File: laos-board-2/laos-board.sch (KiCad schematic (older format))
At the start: 66 parts, among them IC1 KB847, IC2 KB847, J1 CONN_4, J10 MBED NXP, J11 JP_3, J12 POLOLU1201, J13 CONN_5, J14 CONN_4, J15 JP_3, J16 POLOLU1201, J17 CONN_5, J18 CONN_4, J19 CONN_4, J2 JP, J20 JP, J21 JP, J22 CONN_2, J23 CONN_4, J24 CONN_4, J25 JP, J26 CONN_2, J3 CONN_2, J4 USB-A, J5 MAGJACK, J6 JP_3, J7 POLOLU1201, J8 CONN_5, J9 CONN_4, U1 65HVD251, U2 SDCARD, U3 7805

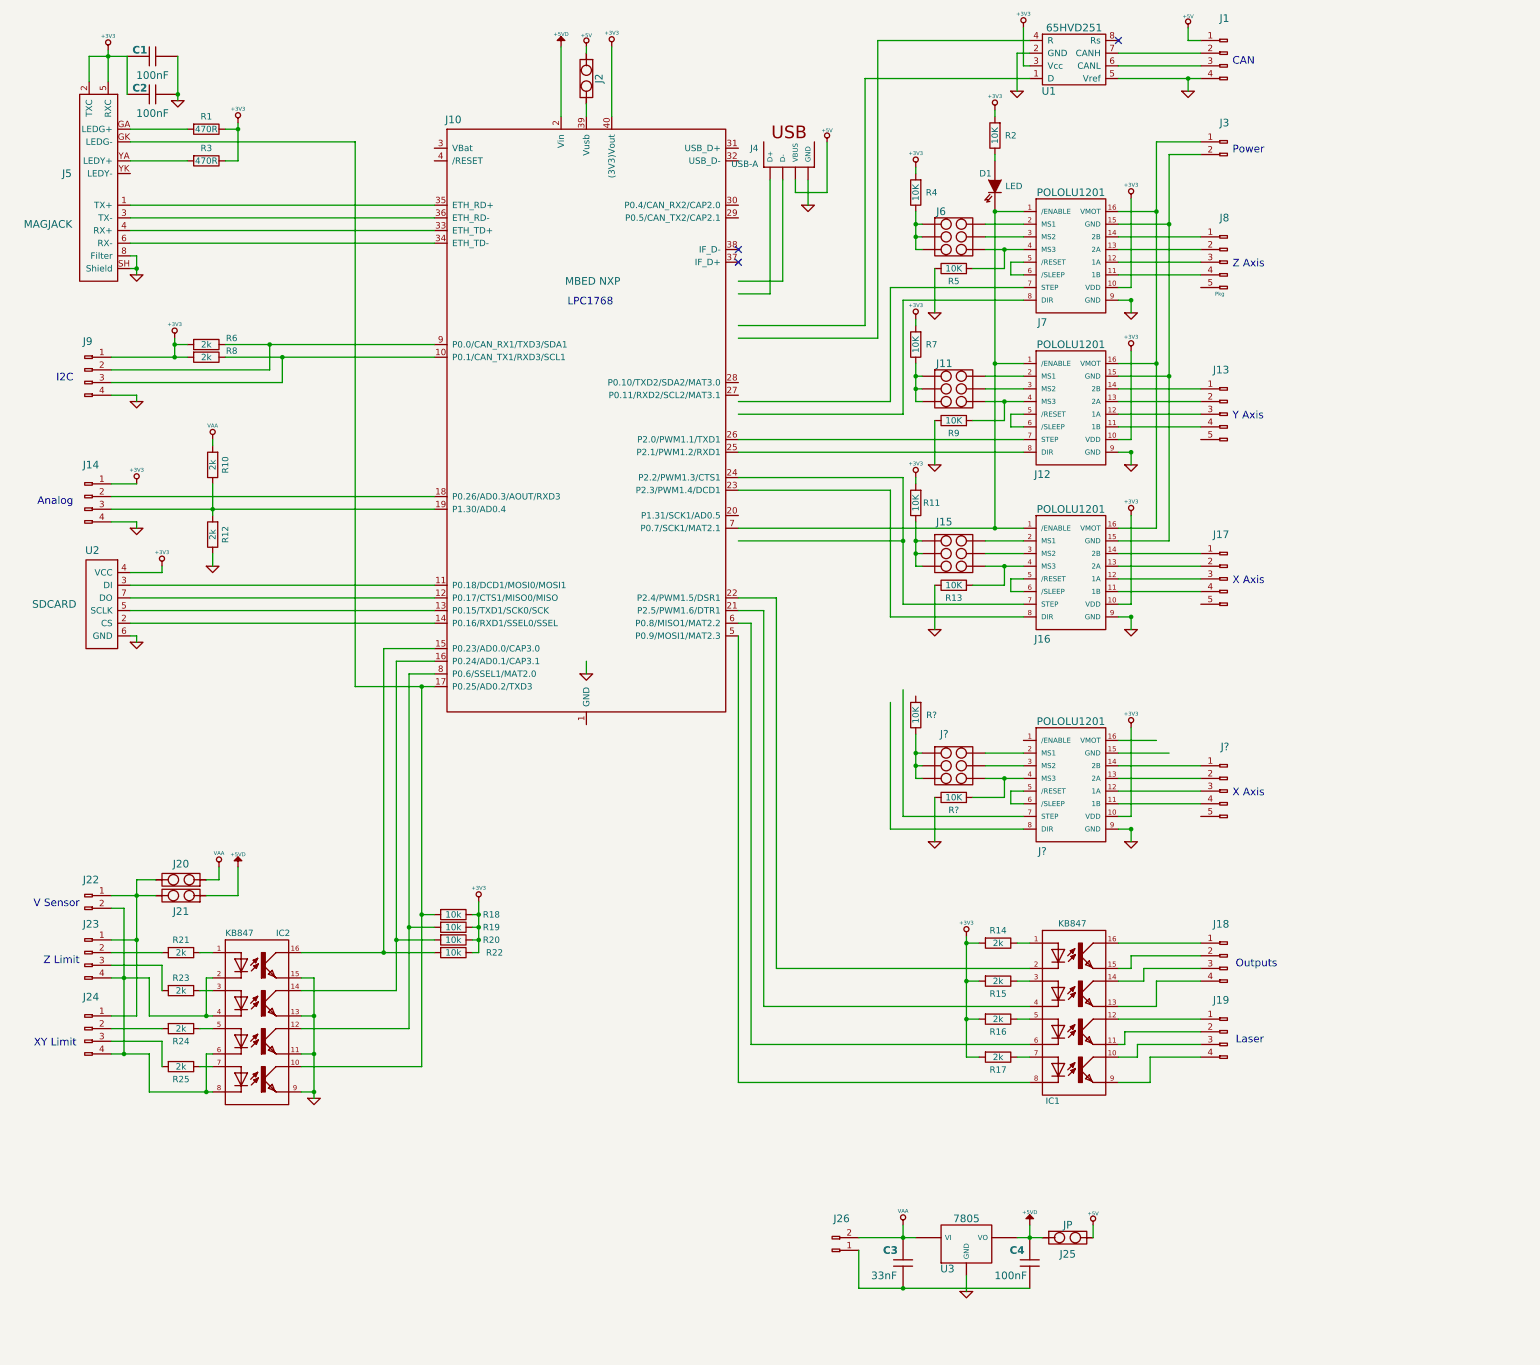
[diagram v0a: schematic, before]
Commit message: Add new polulu and some power nets
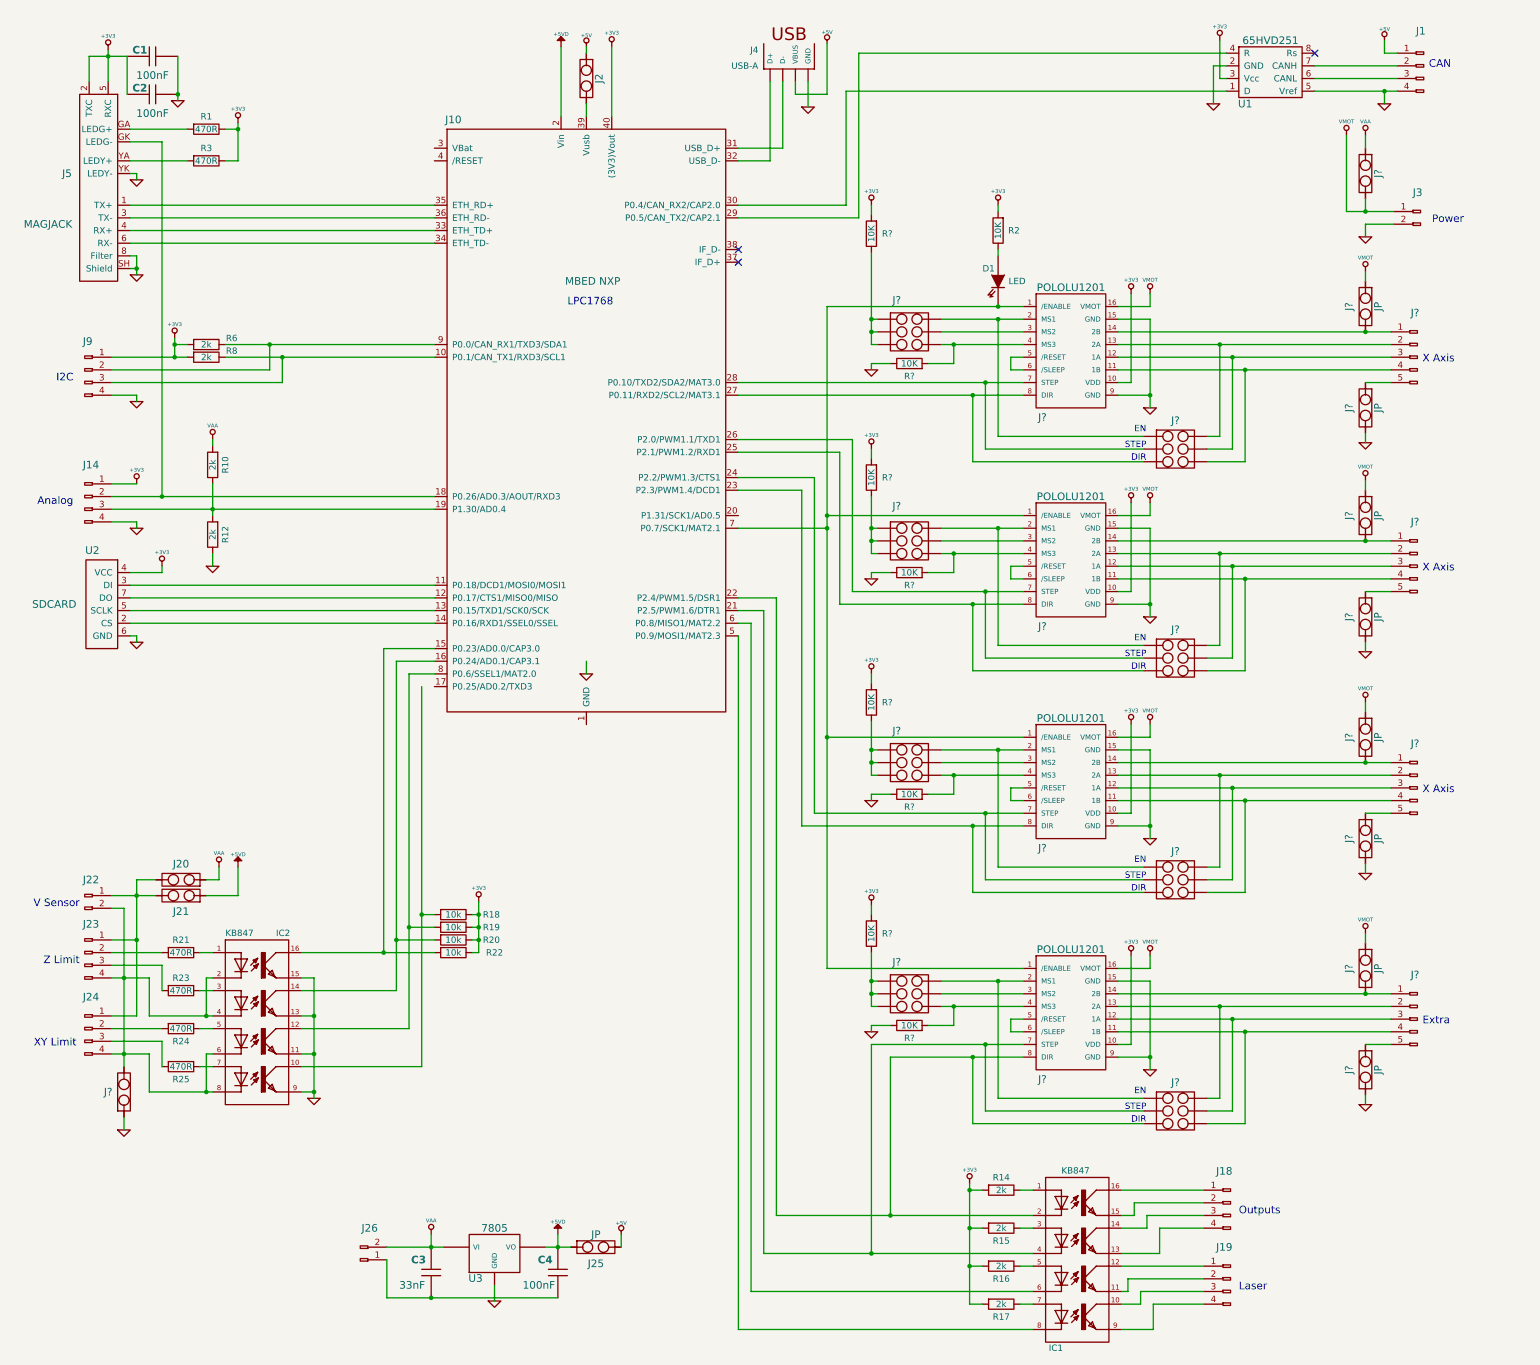
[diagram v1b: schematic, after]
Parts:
- removed J11, J15, J6: JP_3, Pkg, symbol JP_3
- removed J12, J16, J7: POLOLU1201, symbol POLOLU1201
- removed J13, J17, J8: CONN_5, Pkg, symbol CONN_5
- removed R11, R13, R4, R5, R7, R9: 10K, symbol R
- added J? (x10): JP, symbol JP
- added J? (x7): JP_3, Pkg, symbol JP_3
- added J? (x3): POLOLU1201, symbol POLOLU1201
- added J? (x3): CONN_5, Pkg, symbol CONN_5
- added R? (x6): 10K, symbol R
- R21, R23, R24, R25: value 2k -> 470R
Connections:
- net labels added: VMOT
- wire segments 303 -> 377
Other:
- note added: "DIR"
- note added: "EN"
- note added: "Extra"
- note added: "STEP"
- note removed: "Y Axis"
- note removed: "Z Axis"
- moved on the sheet: C3, C4, D1, IC1, J1, J18, J19, J25, J26, J3, J4, J?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

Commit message: Laos board 2 schematic completed before check
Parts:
- added C3: 100nF, Pkg, symbol C
- added C4, C5: 100uF, Pkg, symbol CAP_POL
- gave numbers to parts that had none: 34
- renumbered C3 to C6, C4 to C7, IC2 to IC1, IC1 to IC2, J4 to J1, J9 to J11, J10 to J12, J14 to J15, J1 to J2, J20 to J27, J21 to J29, J2 to J3, J22 to J30, J23 to J31, J24 to J36, J18 to J40, J25 to J41, J26 to J42, J19 to J43, J3 to J6, R12 to R10, R18 to R14, R19 to R15, R20 to R17, R21 to R18, R22 to R19, R3 to R2, R23 to R20, R24 to R22, R25 to R23, R14 to R24, R15 to R25, R16 to R26, R17 to R27, R2 to R3, R6 to R5, R8 to R6, R10 to R8
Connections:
- net GND: now also C3.1, C4.-
- net VMOT: now also C3.2, C4.+
- net at J12.20 (P1.31/SCK1/AD0.5): now also J18.1 (/ENABLE)
- net at D1.2 (K), J12.7 (P0.7/SCK1/MAT2.1), J24.1 (/ENABLE)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: no longer J18.1 (/ENABLE)
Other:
- note added: "Y Axis"
- note added: "Z Axis"
- moved on the sheet: D1, IC2, J10, J13, J14, J16, J17, J18, J19, J2, J20, J21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

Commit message: Updates before pcb design
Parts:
- removed J30: CONN_2, Pkg, symbol CONN_2
- removed J38, J4, J41: JP, symbol JP
- added C?: 100nF, Pkg, symbol C
- added D2: LEDY, symbol LED
- added D3: LEDG, symbol LED
- added J?: CONN_4, Pkg, symbol CONN_4
- added Q? (x2): TIP115, T220-3, symbol TIP115
- added R27, R? (x2): 1k, symbol R
- added R4: 10K, symbol R
- D1: value LED -> LEDR
- R11: renamed from R10; value 2k -> 1k
- R9: renamed from R8; value 2k -> 10k
- renumbered J11 to J10, J12 to J11, J13 to J12, J14 to J13, J15 to J14, J16 to J15, J17 to J16, J18 to J17, J19 to J18, J20 to J19, J21 to J20, J22 to J21, J23 to J22, J24 to J23, J25 to J24, J26 to J25, J27 to J26, J28 to J27, J29 to J28, J31 to J30, J32 to J31, J33 to J32, J34 to J33, J35 to J34, J36 to J35, J37 to J36, J39 to J37, J40 to J38, J42 to J39, J5 to J4, J43 to J40, J6 to J5, J7 to J6, J8 to J7, J9 to J8, J10 to J9, R9 to R10, R11 to R12, R12 to R13, R13 to R14, R14 to R15, R15 to R16, R16 to R17, R17 to R18, R18 to R20, R20 to R21, R21 to R22, R22 to R23, R23 to R24, R24 to R25, R25 to R26, R26 to R28, R27 to R29, R4 to R5, R5 to R6, R6 to R7, R7 to R8
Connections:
- net +5V: now also C7.2, J28.1, U3.3 (VO), R27.1
- net +5VD: no longer C7.2, J28.1, U3.3 (VO)
- net GND: now also J11.1 (GND), J30.4 (P4), J35.4 (P4), C?.1, D2.2 (K), J?.4 (P4), Q?.E, Q?.E
- net VAA: now also C5.+, J39.1 (P1); no longer J39.2 (P2), R9.2
- net VMOT: now also R9.2, R4.2
- net at J11.17 (P0.25/AD0.2/TXD3): now also IC1.10, R15.2
- net at J11.31 (USB_D+): now also J1.D+; no longer J1.D-
- net at J11.32 (USB_D-): now also J1.D-; no longer J1.D+
- net at IC2.8, J11.5 (P0.9/MOSI1/MAT2.3): now also R?.1
- net at IC2.6, J11.6 (P0.8/MISO1/MAT2.2): now also R?.1
- net at C6.1, C7.1: now also C5.-, J39.2 (P2), D3.2 (K); no longer J39.1 (P1)
- net at IC1.1: now also IC1.3 (A), IC1.5, IC1.7, J26.2, J28.2, J30.1 (P1), J35.1 (P1), J?.3 (P3); no longer R20.1
- net at R21.1: now also IC1.4; no longer IC1.3 (A)
- net at R23.1: now also IC1.6; no longer IC1.5
- net at R24.1: now also IC1.8; no longer IC1.7
- new net: IC1.2, R20.1
- new net: D2.1 (A), R4.1
- new net: D3.1 (A), R27.2
- new net: Q?.B, R?.2 (x2)
- new net: J?.2 (P2), Q?.C
- new net: J?.1 (P1), Q?.C
- no-connect marks 3 -> 5
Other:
- note added: "Power 5VIN"
- moved on the sheet: C3, C4, C5, C6, C7, J26, J28, J30, J35, J39, R20, R21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

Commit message: Last minute schematic changes
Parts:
- removed J26, J28: JP, symbol JP
- added J28: JP3, symbol JP3
- added R1: 120R, symbol R
- C4: value 100uF -> 1000uF
- J10: Farnell (none) -> 1234; RS (none) -> 5678
- gave numbers to parts that had none: 6
- renumbered C5 to C6, C6 to C7, C7 to C8, J27 to J26, J30 to J29, J31 to J30, J32 to J31, J33 to J32, J34 to J33, J35 to J34, J36 to J35, J37 to J36, J38 to J37, J39 to J38, J40 to J39, R9 to R10, R10 to R11, R11 to R12, R12 to R13, R13 to R14, R14 to R16, R15 to R18, R16 to R19, R1 to R2, R17 to R20, R18 to R21, R19 to R22, R20 to R23, R21 to R24, R22 to R25, R23 to R26, R24 to R27, R25 to R28, R26 to R29, R2 to R3, R27 to R30, R28 to R31, R29 to R32, R3 to R4, R4 to R5, R5 to R6, R6 to R7, R7 to R8, R8 to R9
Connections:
- net +3V3: no longer J10.1 (P1), R7.2, R8.2
- net +5V: now also J10.1 (P1), R7.2, R8.2, J28.1
- net VAA: now also J28.3
- net at J11.29 (P0.5/CAN_TX2/CAP2.1): now also U1.1 (D); no longer U1.4 (R)
- net at J11.30 (P0.4/CAN_RX2/CAP2.0): now also U1.4 (R); no longer U1.1 (D)
- net at IC1.1, IC1.3 (A), IC1.5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: now also J28.2
- net at J2.2 (P2), U1.7 (CANH): now also R1.2
- net at J2.3 (P3), U1.6 (CANL): now also R1.1
